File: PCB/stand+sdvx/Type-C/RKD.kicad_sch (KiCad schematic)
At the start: 87 parts, among them J1 USB_C_Receptacle_USB2.0, J10 Conn_01x04_Male, J11 Conn_02x06_Odd_Even, J12 Conn_01x06, J13 Conn_01x03, J14 Conn_01x04, J15 Conn_01x04, J2 Conn_02x02_Odd_Even, J3 Conn_02x04_Odd_Even, J4 Conn_02x02_Odd_Even, J5 Conn_02x04_Odd_Even, J6 Conn_02x04_Odd_Even, J7 Conn_02x02_Odd_Even, J8 Conn_02x02_Odd_Even, J9 Conn_02x04_Odd_Even, K1 Key, K2 Key, K3 Key, K4 Key, K5 Key, K6 Key, SW2 SW_DIP_x04, SW3 SW_Push, SW5 SW_Push, SW6 RotaryEncoder_Switch, SW7 SW_Push, SW8 RotaryEncoder_Switch, U1 W25Q32JV, U2 RP2040, U3 CH9329, U4 AMS1117-33, Y1 Crystal 12MHZ HC49, Y2 Crystal_GND24 12MHZ 3225

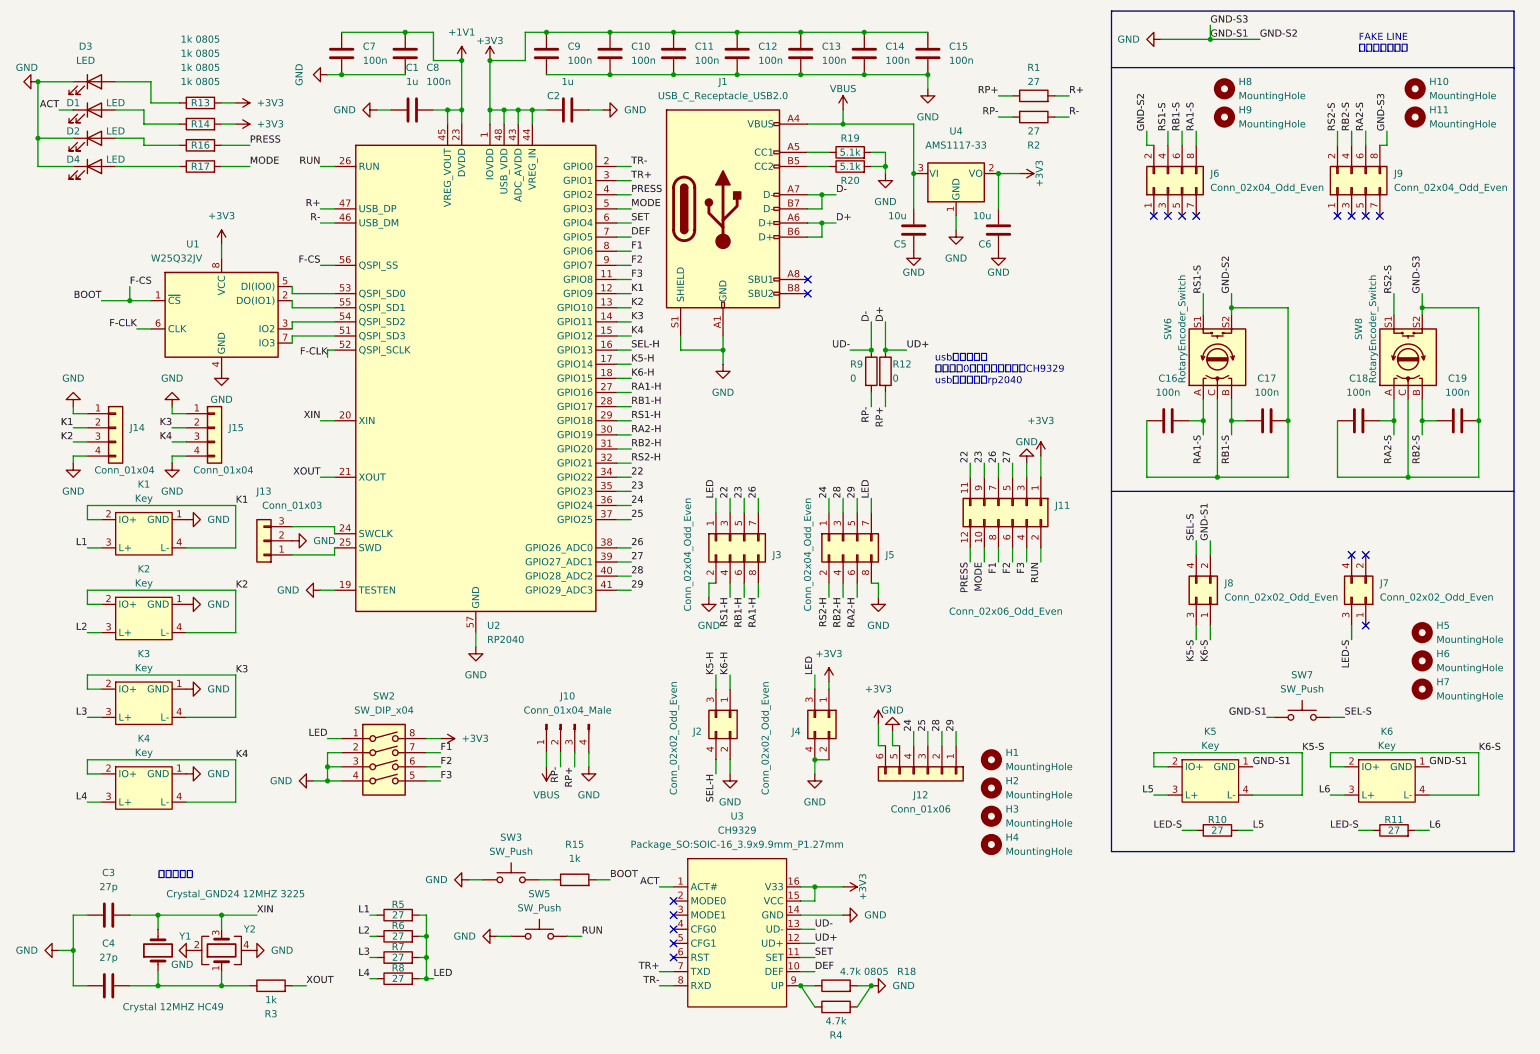
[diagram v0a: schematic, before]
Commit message: 紧急修复:经验证3225晶振无法稳定起振,故去除所以文件中的3225晶振
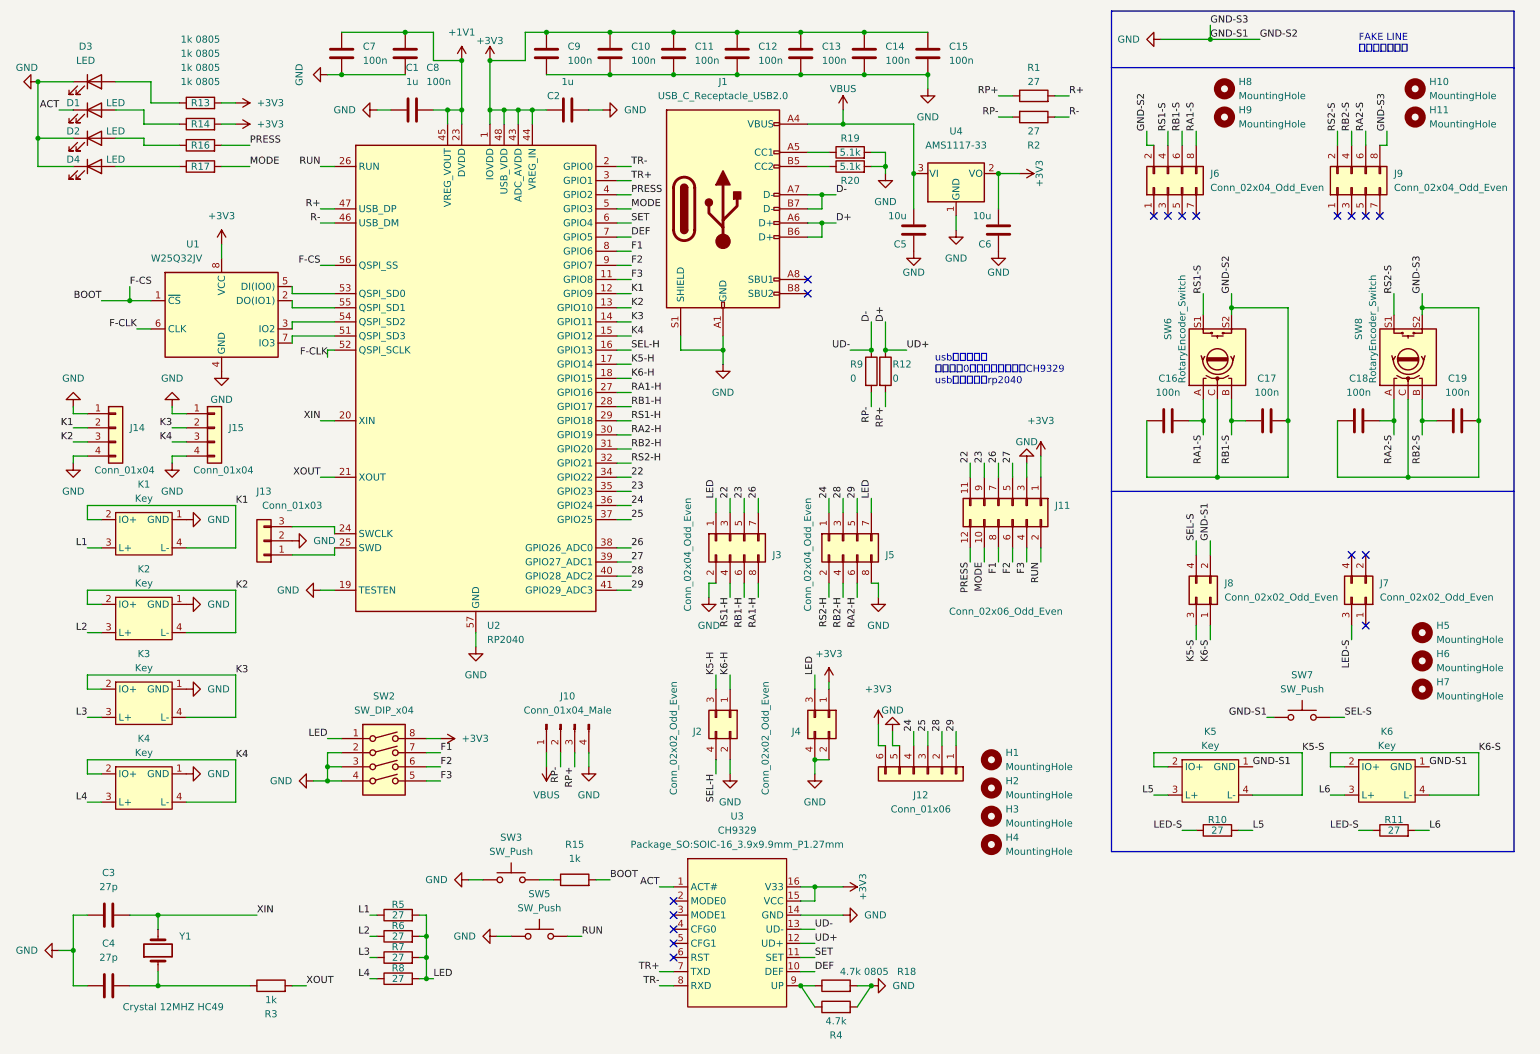
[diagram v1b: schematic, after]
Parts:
- removed Y2: Crystal_GND24 12MHZ 3225, Crystal:Crystal_SMD_3225-4Pin_3.2x2.5mm, symbol Device:Crystal_GND24
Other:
- note removed: "晶振二选一"

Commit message: rename
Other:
- company: PCX-LK -> PTALTS-LK

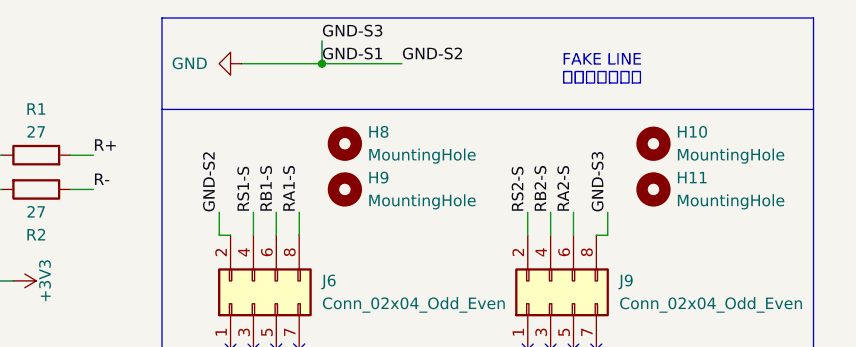
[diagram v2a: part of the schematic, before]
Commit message: 更新,py代码重构,sdvx版pcb修改
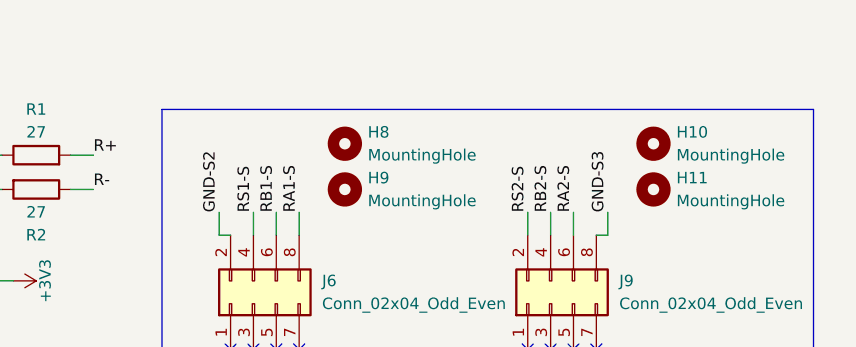
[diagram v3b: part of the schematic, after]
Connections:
- net GND: no longer C16.2, C17.1, C18.2, C19.1, J6.2 (Pin_2), J8.2 (Pin_2), J9.8 (Pin_8), K5.1 (GND), K6.1 (GND), SW6.C, SW6.S2, SW7.1, SW8.C, SW8.S2
- new net GND-S1: J8.2 (Pin_2), K5.1 (GND), K6.1 (GND), SW7.1
- new net GND-S2: C16.2, C17.1, J6.2 (Pin_2), SW6.C, SW6.S2
- new net GND-S3: C18.2, C19.1, J9.8 (Pin_8), SW8.C, SW8.S2
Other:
- note removed: "FAKE LINE 特殊目的用连线"
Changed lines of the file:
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@@
   (title_block
     (title "RKD-TypeC-SDVX")
-    (date "2023-08-20")
-    (rev "38")
+    (date "2023-11-26")
+    (rev "39")
     (company "PTALTS-LK")
     (comment 1 "https://github.com/PTALTS-LK/RKD")
@@
   (junction (at 157.48 170.18) (diameter 0) (color 0 0 0 0)
   )
-  (junction (at 228.6 17.78) (diameter 0) (color 0 0 0 0)
-  )
   (junction (at 83.82 16.51) (diameter 0) (color 0 0 0 0)
   )
@@
     (stroke (width 0) (type default))
   )
-  (polyline (pts (xy 283.21 12.7) (xy 283.21 22.86))
-    (stroke (width 0) (type default))
-  )
   (wire (pts (xy 170.18 38.1) (xy 170.18 40.64))
     (stroke (width 0) (type default))
@@
     (stroke (width 0) (type default))
   )
-  (polyline (pts (xy 210.82 12.7) (xy 283.21 12.7))
-    (stroke (width 0) (type default))
-  )
   (wire (pts (xy 71.12 68.58) (xy 63.5 68.58))
     (stroke (width 0) (type default))
@@
     (stroke (width 0) (type default))
   )
-  (wire (pts (xy 228.6 15.24) (xy 228.6 17.78))
-    (stroke (width 0) (type default))
-  )
   (wire (pts (xy 24.13 175.26) (xy 24.13 181.61))
     (stroke (width 0) (type default))
@@
     (stroke (width 0) (type default))
   )
-  (wire (pts (xy 228.6 17.78) (xy 237.49 17.78))
-    (stroke (width 0) (type default))
-  )
   (wire (pts (xy 175.26 41.91) (xy 175.26 48.26))
     (stroke (width 0) (type default))
@@
     (stroke (width 0) (type default))
   )
-  (wire (pts (xy 219.71 17.78) (xy 228.6 17.78))
-    (stroke (width 0) (type default))
-  )
   (wire (pts (xy 167.64 81.28) (xy 167.64 83.82))
     (stroke (width 0) (type default))
@@
     (stroke (width 0) (type default))
   )
-  (polyline (pts (xy 210.82 22.86) (xy 210.82 12.7))
-    (stroke (width 0) (type default))
-  )
   (wire (pts (xy 190.5 27.94) (xy 193.04 27.94))
     (stroke (width 0) (type default))
@@
     (effects (font (size 1.27 1.27)) (justify left bottom))
   )
-  (text "FAKE LINE\n特殊目的用连线" (at 255.27 20.32 0)
-    (effects (font (size 1.27 1.27)) (justify left bottom))
-  )
   (label "RUN" (at 68.58 40.64 180) (fields_autoplaced)
     (effects (font (size 1.27 1.27)) (justify right bottom))
@@
     (effects (font (size 1.27 1.27)) (justify right bottom))
   )
-  (label "GND-S3" (at 228.6 15.24 0) (fields_autoplaced)
-    (effects (font (size 1.27 1.27)) (justify left bottom))
-  )
   (label "29" (at 124.46 116.84 0) (fields_autoplaced)
     (effects (font (size 1.27 1.27)) (justify left bottom))
@@
     (effects (font (size 1.27 1.27)) (justify left bottom))
   )
-  (label "GND-S1" (at 228.6 17.78 0) (fields_autoplaced)
-    (effects (font (size 1.27 1.27)) (justify left bottom))
-  )
   (label "23" (at 124.46 99.06 0) (fields_autoplaced)
     (effects (font (size 1.27 1.27)) (justify left bottom))
@@
     (effects (font (size 1.27 1.27)) (justify right bottom))
   )
-  (label "GND-S2" (at 237.49 17.78 0) (fields_autoplaced)
-    (effects (font (size 1.27 1.27)) (justify left bottom))
-  )
   (label "RUN" (at 198.12 111.76 270) (fields_autoplaced)
     (effects (font (size 1.27 1.27)) (justify right bottom))
@@
         )
       )
-    )
-  )
-  (symbol (lib_name "GND_1") (lib_id "power:GND") (at 219.71 17.78 270) (unit 1)
-    (in_bom yes) (on_board yes) (dnp no) (fields_autoplaced)
-    (property "Reference" "#PWR0142" (at 213.36 17.78 0)
-      (effects (font (size 1.27 1.27)) hide)
-    )
-    (property "Value" "GND" (at 215.9 17.7799 90)
-      (effects (font (size 1.27 1.27)) (justify right))
-    )
-    (property "Footprint" "" (at 219.71 17.78 0)
-      (effects (font (size 1.27 1.27)) hide)
-    )
-    (property "Datasheet" "" (at 219.71 17.78 0)
-      (effects (font (size 1.27 1.27)) hide)
-    )
-    (pin "1")
-    (instances
-      (project "RKD"
-        (path "/638016c8-c1db-4492-a113-b4cbe1731dad"
-          (reference "#PWR0142") (unit 1)
-        )
-      )
